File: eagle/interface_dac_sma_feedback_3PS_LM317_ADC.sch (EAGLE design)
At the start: 43 parts, among them IC1 ISO1540, IC2 LT1352PA, IC3 LT1352PA, IC4 LM317MABDT, IC5 LM317MABDT, IC6 LM317MABDT, Q1 TIP122V, Q2 TIP122V, Q3 TIP122V, X1 BU-SMA-V

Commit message: Readbacks
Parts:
- removed HVRDOUT+, HVRDOUT-, HVRDOUTCT: (no value), con-molex:KK-156-3
- added U$3: ADS1015DIL, texas:ADS1015DIL
- C1: device rcl:C-US050-050X075 -> rcl:C-US050-024X044
- C4: device resistor:C-US075-063X106 -> resistor:C-US050-024X044
- C7: device resistor:C-US050-050X075 -> resistor:C-US050-024X044
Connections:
- removed net N$27: IC3A.-IN, R13.2, R9.1
- removed net N$6: FDBKHV-2.S, HVRDOUTCT-2.S, IC2B.-IN, R4.1
- removed net N$8: FDBKHV-1.S, HVRDOUT+-2.S, IC2A.-IN, R3.1
- new net RDBK1: FDBKHV-1.S, IC2A.-IN, R3.1, U$3.AIN0
- new net RDBK2: FDBKHV-2.S, IC2B.-IN, R4.1, U$3.AIN1
- new net RDBK3: IC3A.-IN, R13.2, R9.1, U$3.AIN2
- new net RDBK4: C2.1, U$1.P$1, U$3.AIN3
- net +12V: no longer HVRDOUT+-1.S, HVRDOUT--1.S, HVRDOUTCT-1.S
- net GND: now also U$3.ADDR, U$3.GND; no longer HVRDOUT+-3.S, HVRDOUT--3.S, HVRDOUTCT-3.S
- net N$14: no longer HVRDOUT--2.S
- net N$2: no longer C2.1, U$1.P$1
- net SCL_OUT: now also U$3.SCL
- net SDA_OUT: now also U$3.SDA
- net VCC: now also U$3.VDD
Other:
- moved on the sheet: C7, IC1, POWERINTERFACE-1, POWERINTERFACE-2, POWERINTERFACE-3, POWERINTERFACE-4, R1, R2

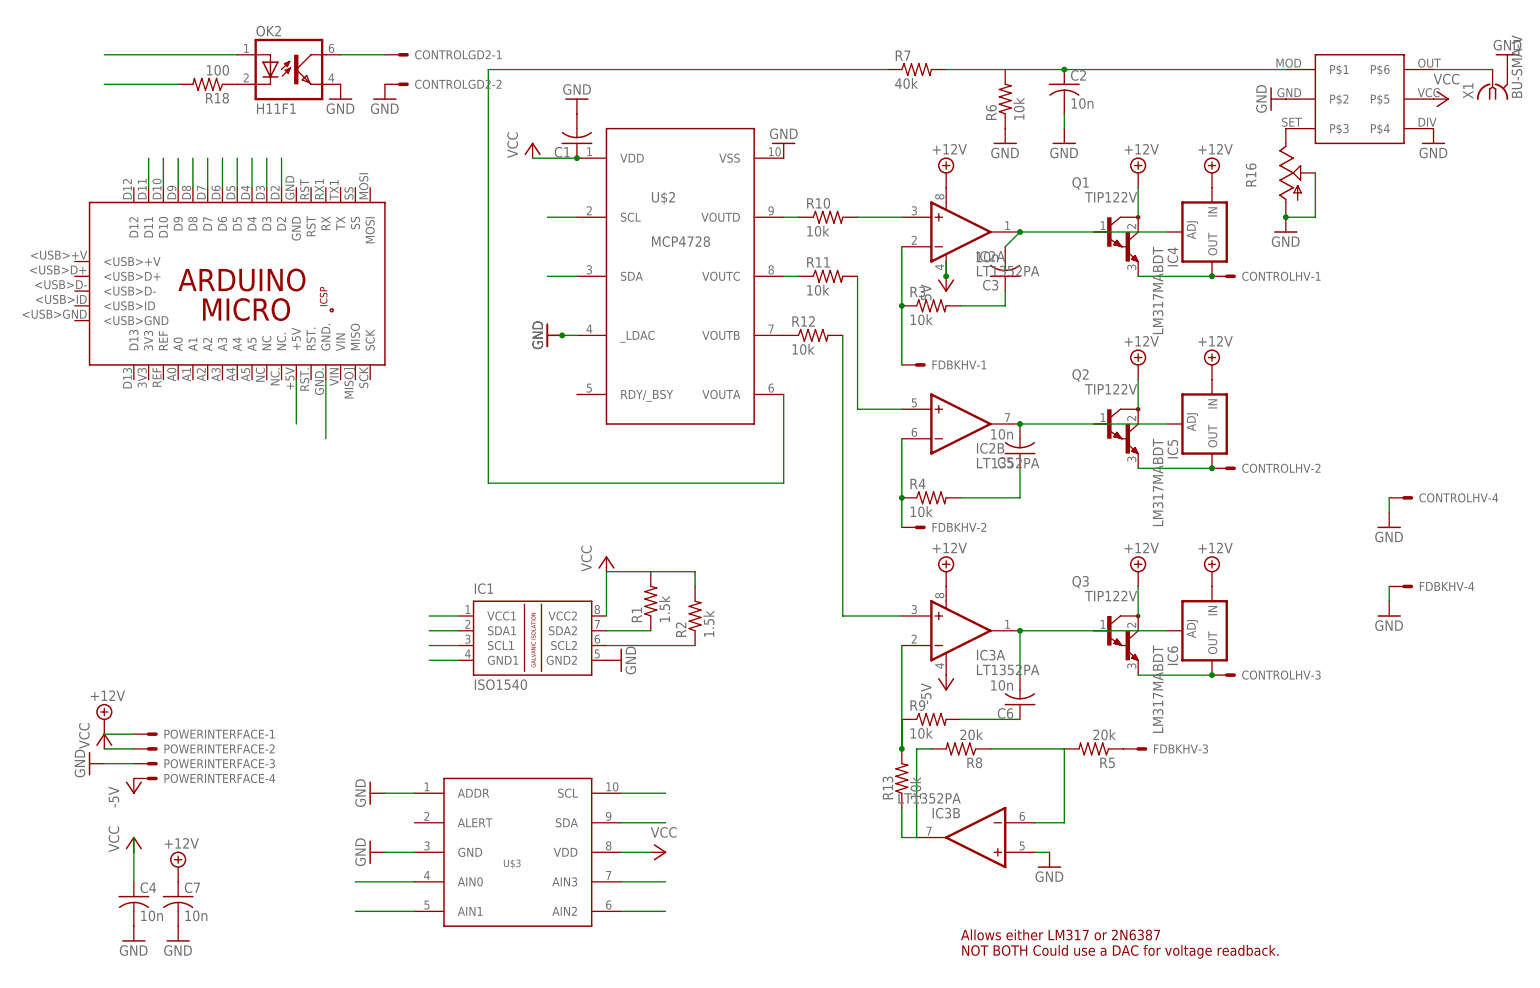
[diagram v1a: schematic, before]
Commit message: Add adc
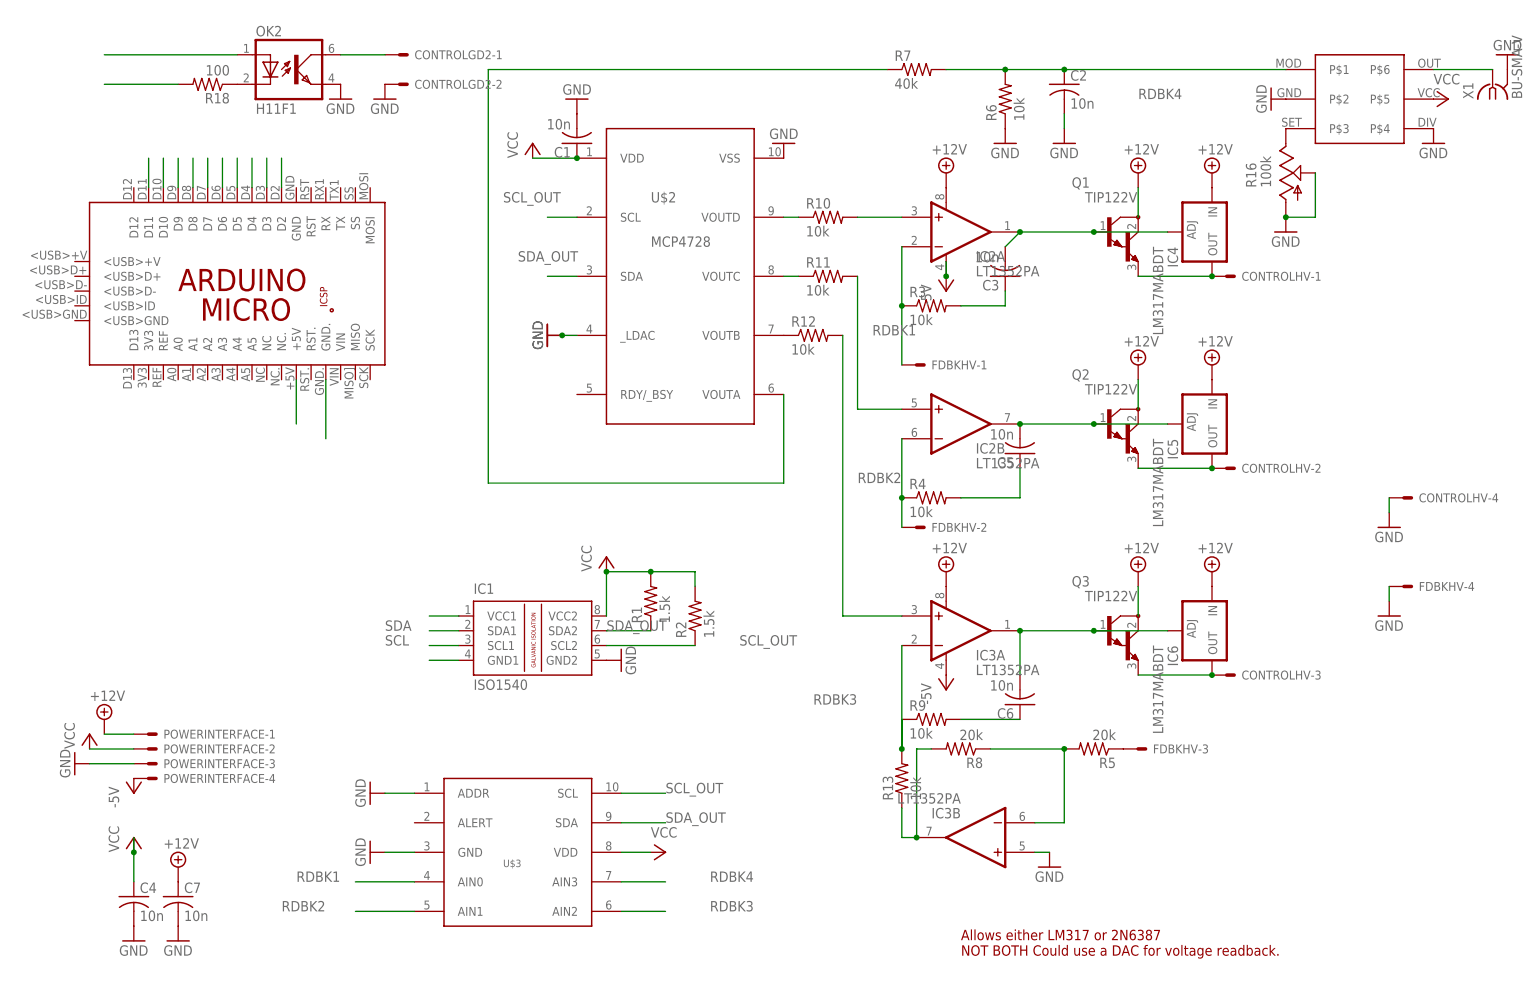
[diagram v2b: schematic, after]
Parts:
- C1: value (none) -> 10n
- R16: value (none) -> 100k
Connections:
- removed net N$2: R6.2, R7.2
- net RDBK4: now also R6.2, R7.2
